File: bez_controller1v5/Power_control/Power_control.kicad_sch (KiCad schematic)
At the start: 7 parts, among them J1 Screw_Terminal_01x02, J2 Screw_Terminal_01x02, J3 Screw_Terminal_01x02, Q2 IRF4905STRLPBF

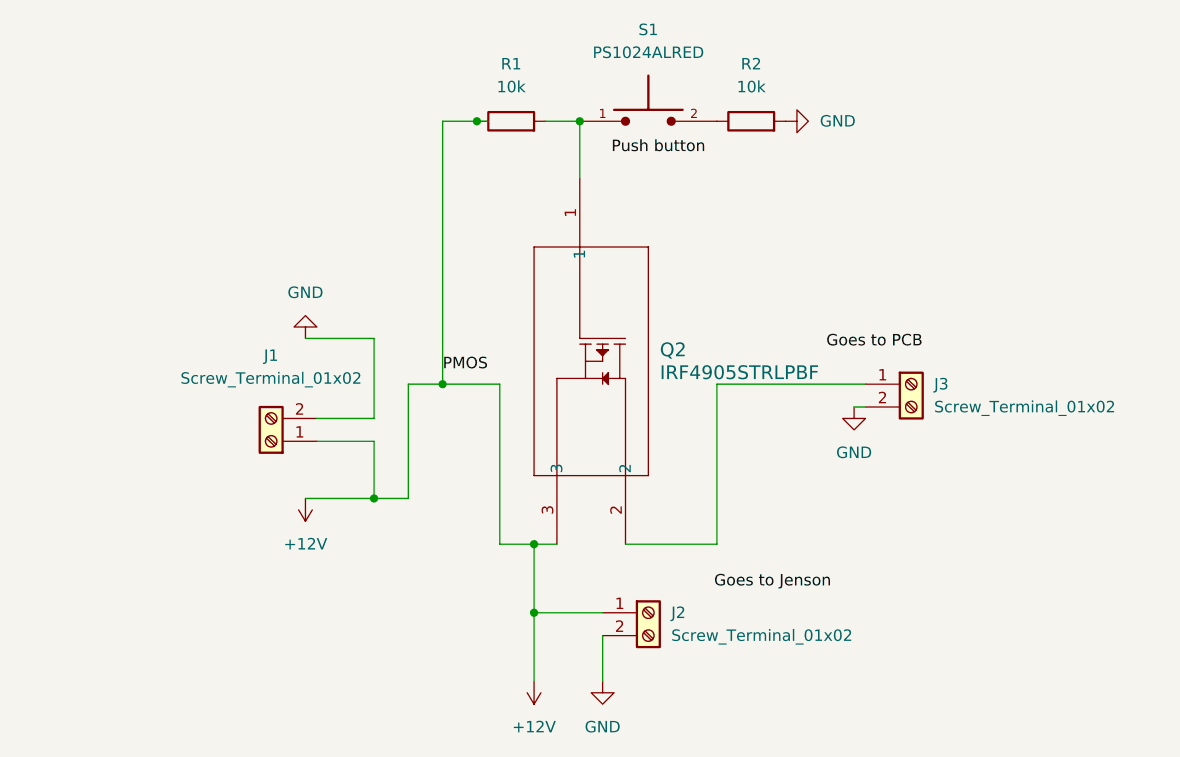
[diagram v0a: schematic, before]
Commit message: Cleaned circuit up a little
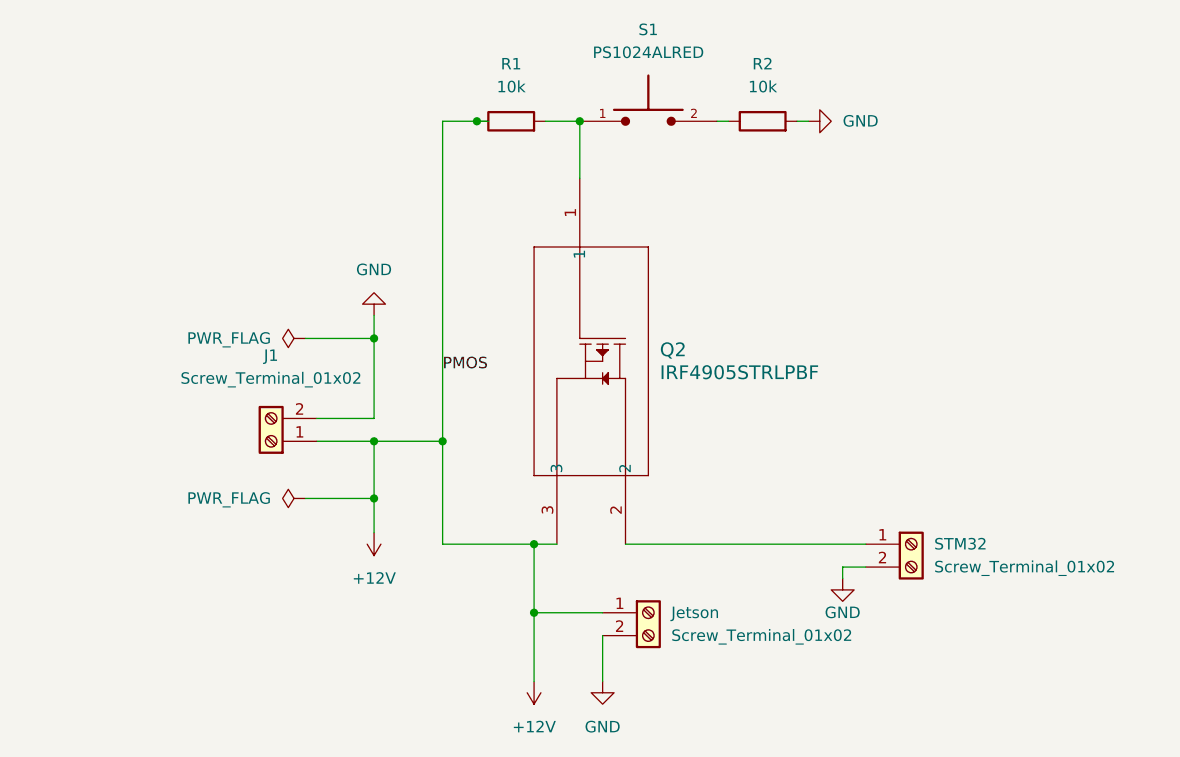
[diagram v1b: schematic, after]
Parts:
- renumbered J2 to Jetson, J3 to STM32
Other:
- moved on the sheet: R2, STM32

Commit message: Made foorprints and PCB for button
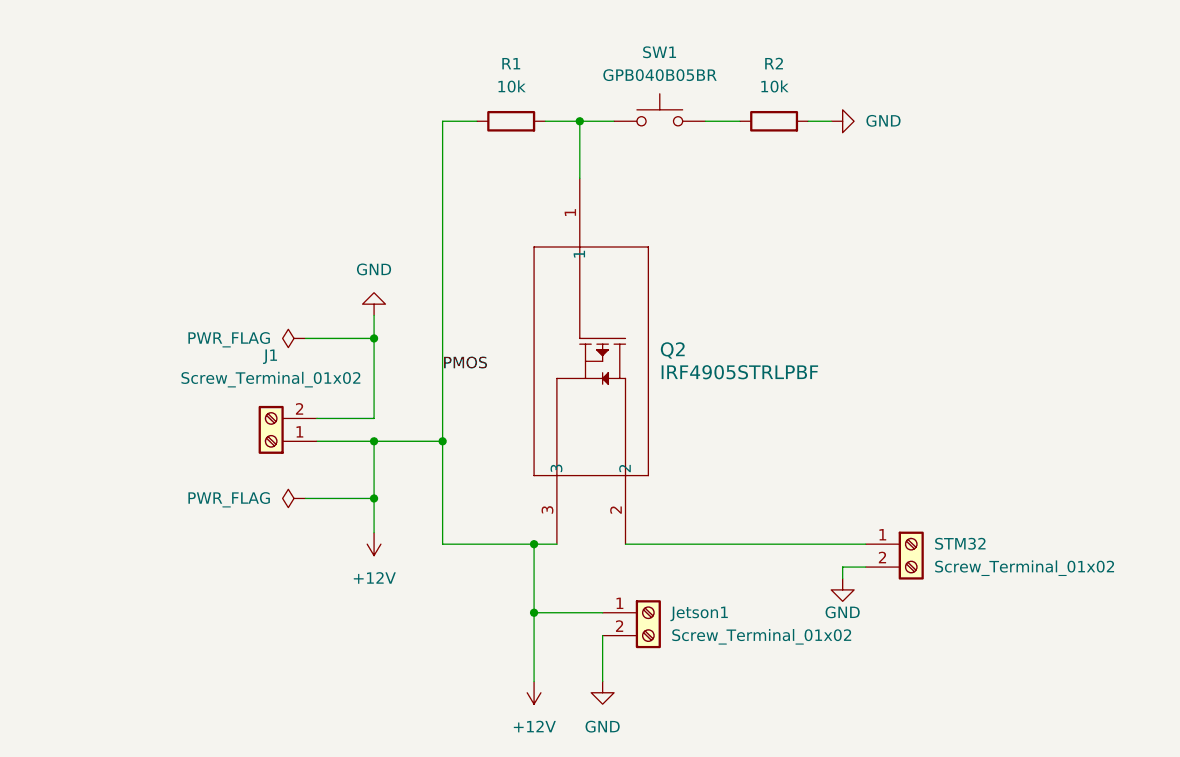
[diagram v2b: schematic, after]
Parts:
- removed S1: PS1024ALRED, PS1024ALRED:SW_PS1024ALRED, symbol PS1024ALRED:PS1024ALRED
- added SW1: GPB040B05BR, Library:GPB040B05BR, symbol Switch:SW_Push
- Q2: footprint TRAN_IRF4905STRLPBF_INF -> Library:IRF4905
- R1, R2: footprint (none) -> Resistor_SMD:R_0603_1608Metric
- renumbered Jetson to Jetson1
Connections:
- net at Q2.1, R1.2: now also SW1.1
- net at R2.1: now also SW1.2
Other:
- moved on the sheet: R2
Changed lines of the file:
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@@
 		(color 0 0 0 0)
 	)
-	(junction
-		(at 81.28 52.07)
-		(diameter 0)
-		(color 0 0 0 0)
-	)
 	(wire
 		(pts
@@
 	(wire
 		(pts
-			(xy 82.55 52.07) (xy 81.28 52.07)
-		)
-		(stroke
-			(width 0)
-			(type default)
-		)
-	)
-	(wire
-		(pts
 			(xy 87.63 106.68) (xy 87.63 99.06)
 		)
@@
 	(wire
 		(pts
+			(xy 120.65 52.07) (xy 118.11 52.07)
+		)
+		(stroke
+			(width 0)
+			(type default)
+		)
+	)
+	(wire
+		(pts
 			(xy 69.85 87.63) (xy 63.5 87.63)
 		)
@@
 	(wire
 		(pts
-			(xy 109.22 52.07) (xy 107.95 52.07)
-		)
-		(stroke
-			(width 0)
-			(type default)
-		)
-	)
-	(wire
-		(pts
 			(xy 69.85 93.98) (xy 69.85 97.79)
 		)
@@
 	(wire
 		(pts
-			(xy 116.84 52.07) (xy 118.11 52.07)
+			(xy 92.71 52.07) (xy 92.71 58.42)
 		)
 		(stroke
@@
 	(wire
 		(pts
+			(xy 106.68 52.07) (xy 110.49 52.07)
+		)
+		(stroke
+			(width 0)
+			(type default)
+		)
+	)
+	(wire
+		(pts
 			(xy 69.85 87.63) (xy 77.47 87.63)
 		)
@@
 	(wire
 		(pts
+			(xy 92.71 52.07) (xy 96.52 52.07)
+		)
+		(stroke
+			(width 0)
+			(type default)
+		)
+	)
+	(wire
+		(pts
 			(xy 81.28 52.07) (xy 77.47 52.07)
 		)
@@
 		(pts
 			(xy 62.23 76.2) (xy 69.85 76.2)
-		)
-		(stroke
-			(width 0)
-			(type default)
-		)
-	)
-	(wire
-		(pts
-			(xy 92.71 58.42) (xy 92.71 52.07)
 		)
 		(stroke
@@
 	)
 	(symbol
-		(lib_id "PS1024ALRED:PS1024ALRED")
-		(at 100.33 52.07 0)
-		(unit 1)
-		(exclude_from_sim no)
-		(in_bom yes)
-		(on_board yes)
-		(dnp no)
-		(fields_autoplaced yes)
-		(property "Reference" "S1"
-			(at 100.33 41.91 0)
-			(effects
-				(font
-					(size 1.27 1.27)
-				)
-			)
-		)
-		(property "Value" "PS1024ALRED"
-			(at 100.33 44.45 0)
-			(effects
-				(font
-					(size 1.27 1.27)
-				)
-			)
-		)
-		(property "Footprint" "PS1024ALRED:SW_PS1024ALRED"
-			(at 100.33 52.07 0)
-			(effects
-				(font
-					(size 1.27 1.27)
-				)
-				(justify bottom)
-				(hide yes)
-			)
-		)
-		(property "Datasheet" ""
-			(at 100.33 52.07 0)
-			(effects
-				(font
-					(size 1.27 1.27)
-				)
-				(hide yes)
-			)
-		)
-		(property "Description" ""
-			(at 100.33 52.07 0)
-			(effects
-				(font
-					(size 1.27 1.27)
-				)
-				(hide yes)
-			)
-		)
-		(property "PARTREV" "C"
-			(at 100.33 52.07 0)
-			(effects
-				(font
-					(size 1.27 1.27)
-				)
-				(justify bottom)
-				(hide yes)
-			)
-		)
-		(property "STANDARD" "IPC-7351B"
-			(at 100.33 52.07 0)
-			(effects
-				(font
-					(size 1.27 1.27)
-				)
-				(justify bottom)
-				(hide yes)
-			)
-		)
-		(property "MAXIMUM_PACKAGE_HEIGHT" "26.6 mm"
-			(at 100.33 52.07 0)
-			(effects
-				(font
-					(size 1.27 1.27)
-				)
-				(justify bottom)
-				(hide yes)
-			)
-		)
-		(property "MANUFACTURER" "E-Switch"
-			(at 100.33 52.07 0)
-			(effects
-				(font
-					(size 1.27 1.27)
-				)
-				(justify bottom)
-				(hide yes)
-			)
-		)
-		(pin "1"
-		)
-		(pin "2"
-		)
-		(instances
-			(project "Power_control"
-				(path "/56259e4c-5c8f-4073-95b8-1c3757b66f06"
-					(reference "S1")
-					(unit 1)
-				)
-			)
-		)
-	)
-	(symbol
 		(lib_id "Connector:Screw_Terminal_01x02")
 		(at 58.42 87.63 180)
@@
 			)
 		)
-		(property "Footprint" ""
+		(property "Footprint" "Resistor_SMD:R_0603_1608Metric"
 			(at 85.09 53.848 90)
 			(effects
@@
 	(symbol
 		(lib_id "power:GND")
-		(at 118.11 52.07 90)
+		(at 120.65 52.07 90)
 		(unit 1)
 		(exclude_from_sim no)
@@
 		(fields_autoplaced yes)
 		(property "Reference" "#PWR04"
-			(at 124.46 52.07 0)
+			(at 127 52.07 0)
 			(effects
 				(font
@@
 		)
 		(property "Value" "GND"
-			(at 121.92 52.0699 90)
+			(at 124.46 52.0699 90)
 			(effects
 				(font
@@
 		)
 		(property "Footprint" ""
-			(at 118.11 52.07 0)
+			(at 120.65 52.07 0)
 			(effects
 				(font
@@
 		)
 		(property "Datasheet" ""
-			(at 118.11 52.07 0)
+			(at 120.65 52.07 0)
 			(effects
 				(font
@@
 		)
 		(property "Description" "Power symbol creates a global label with name \"GND\" , ground"
-			(at 118.11 52.07 0)
+			(at 120.65 52.07 0)
 			(effects
 				(font
@@
 				(path "/56259e4c-5c8f-4073-95b8-1c3757b66f06"
 					(reference "#PWR04")
+					(unit 1)
+				)
+			)
+		)
+	)
+	(symbol
+		(lib_id "Switch:SW_Push")
+		(at 101.6 52.07 0)
+		(unit 1)
+		(exclude_from_sim no)
+		(in_bom yes)
+		(on_board yes)
+		(dnp no)
+		(fields_autoplaced yes)
+		(property "Reference" "SW1"
+			(at 101.6 44.45 0)
+			(effects
+				(font
+					(size 1.27 1.27)
+				)
+			)
+		)
+		(property "Value" "GPB040B05BR"
+			(at 101.6 46.99 0)
+			(effects
+				(font
+					(size 1.27 1.27)
+				)
+			)
+		)
+		(property "Footprint" "Library:GPB040B05BR"
+			(at 101.6 46.99 0)
+			(effects
+				(font
+					(size 1.27 1.27)
+				)
+				(hide yes)
+			)
+		)
+		(property "Datasheet" "~"
+			(at 101.6 46.99 0)
+			(effects
+				(font
+					(size 1.27 1.27)
+				)
+				(hide yes)
+			)
+		)
+		(property "Description" "Push button switch, generic, two pins"
+			(at 101.6 52.07 0)
+			(effects
+				(font
+					(size 1.27 1.27)
+				)
+				(hide yes)
+			)
+		)
+		(pin "1"
+		)
+		(pin "2"
+		)
+		(instances
+			(project ""
+				(path "/56259e4c-5c8f-4073-95b8-1c3757b66f06"
+					(reference "SW1")
 					(unit 1)
 				)
@@
 		(dnp no)
 		(fields_autoplaced yes)
-		(property "Reference" "Jetson"
+		(property "Reference" "Jetson1"
 			(at 102.87 106.6799 0)
 			(effects
@@
 			(project "Power_control"
 				(path "/56259e4c-5c8f-4073-95b8-1c3757b66f06"
-					(reference "Jetson")
+					(reference "Jetson1")
 					(unit 1)
 				)
@@
 	(symbol
 		(lib_id "Device:R")
-		(at 113.03 52.07 90)
+		(at 114.3 52.07 90)
 		(unit 1)
 		(exclude_from_sim no)
@@
 		(fields_autoplaced yes)
 		(property "Reference" "R2"
-			(at 113.03 45.72 90)
+			(at 114.3 45.72 90)
 			(effects
 				(font
@@
 		)
 		(property "Value" "10k"
-			(at 113.03 48.26 90)
-			(effects
-				(font
-					(size 1.27 1.27)
-				)
-			)
-		)
-		(property "Footprint" ""
-			(at 113.03 53.848 90)
+			(at 114.3 48.26 90)
+			(effects
+				(font
+					(size 1.27 1.27)
+				)
+			)
+		)
+		(property "Footprint" "Resistor_SMD:R_0603_1608Metric"
+			(at 114.3 53.848 90)
 			(effects
 				(font
@@
 		)
 		(property "Datasheet" "~"
-			(at 113.03 52.07 0)
+			(at 114.3 52.07 0)
 			(effects
 				(font
@@
 		)
 		(property "Description" "Resistor"
-			(at 113.03 52.07 0)
+			(at 114.3 52.07 0)
 			(effects
 				(font
@@
 			)
 		)
-		(property "Footprint" "TRAN_IRF4905STRLPBF_INF"
+		(property "Footprint" "Library:IRF4905"
 			(at 95.25 58.42 0)
 			(effects

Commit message: Fixed XT60 polarity
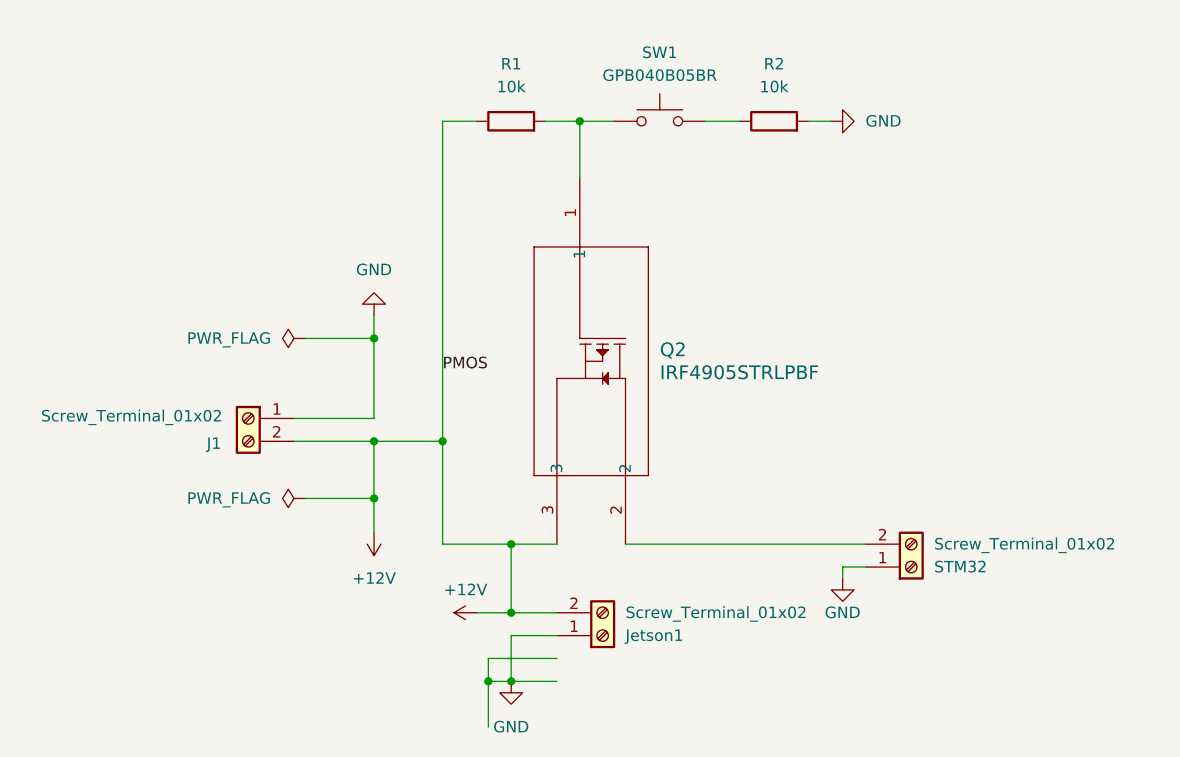
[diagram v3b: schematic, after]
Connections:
- net +12V: now also J1.2 (Pin_2), Jetson1.2 (Pin_2); no longer J1.1 (Pin_1), Jetson1.1 (Pin_1)
- net GND: now also J1.1 (Pin_1), Jetson1.1 (Pin_1), STM32.1 (Pin_1); no longer J1.2 (Pin_2), Jetson1.2 (Pin_2), STM32.2 (Pin_2)
- net at Q2.2: now also STM32.2 (Pin_2); no longer STM32.1 (Pin_1)
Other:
- moved on the sheet: J1, Jetson1
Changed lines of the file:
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@@
 	(paper "A4")
+	(junction
+		(at 82.55 114.3)
+		(diameter 0)
+		(color 0 0 0 0)
+	)
 	(junction
 		(at 77.47 87.63)
@@
 	)
 	(junction
-		(at 87.63 106.68)
+		(at 69.85 87.63)
 		(diameter 0)
 		(color 0 0 0 0)
@@
 	)
 	(junction
-		(at 87.63 99.06)
+		(at 85.09 114.3)
 		(diameter 0)
 		(color 0 0 0 0)
 	)
 	(junction
-		(at 69.85 87.63)
+		(at 85.09 106.68)
+		(diameter 0)
+		(color 0 0 0 0)
+	)
+	(junction
+		(at 85.09 99.06)
 		(diameter 0)
 		(color 0 0 0 0)
@@
 	(wire
 		(pts
-			(xy 87.63 106.68) (xy 87.63 114.3)
-		)
-		(stroke
-			(width 0)
-			(type default)
-		)
-	)
-	(wire
-		(pts
-			(xy 87.63 106.68) (xy 87.63 99.06)
+			(xy 85.09 99.06) (xy 90.17 99.06)
+		)
+		(stroke
+			(width 0)
+			(type default)
+		)
+	)
+	(wire
+		(pts
+			(xy 85.09 99.06) (xy 85.09 106.68)
 		)
 		(stroke
@@
 	(wire
 		(pts
-			(xy 69.85 87.63) (xy 63.5 87.63)
+			(xy 82.55 111.76) (xy 82.55 114.3)
+		)
+		(stroke
+			(width 0)
+			(type default)
+		)
+	)
+	(wire
+		(pts
+			(xy 82.55 114.3) (xy 82.55 119.38)
+		)
+		(stroke
+			(width 0)
+			(type default)
+		)
+	)
+	(wire
+		(pts
+			(xy 97.79 99.06) (xy 124.46 99.06)
 		)
 		(stroke
@@
 	(wire
 		(pts
-			(xy 77.47 99.06) (xy 87.63 99.06)
-		)
-		(stroke
-			(width 0)
-			(type default)
-		)
-	)
-	(wire
-		(pts
-			(xy 97.79 99.06) (xy 124.46 99.06)
+			(xy 77.47 99.06) (xy 85.09 99.06)
 		)
 		(stroke
@@
 	(wire
 		(pts
+			(xy 60.96 85.09) (xy 69.85 85.09)
+		)
+		(stroke
+			(width 0)
+			(type default)
+		)
+	)
+	(wire
+		(pts
 			(xy 69.85 87.63) (xy 77.47 87.63)
 		)
@@
 	(wire
 		(pts
-			(xy 87.63 99.06) (xy 90.17 99.06)
+			(xy 121.92 101.6) (xy 124.46 101.6)
+		)
+		(stroke
+			(width 0)
+			(type default)
+		)
+	)
+	(wire
+		(pts
+			(xy 85.09 114.3) (xy 85.09 109.22)
 		)
 		(stroke
@@
 	(wire
 		(pts
+			(xy 82.55 114.3) (xy 85.09 114.3)
+		)
+		(stroke
+			(width 0)
+			(type default)
+		)
+	)
+	(wire
+		(pts
 			(xy 77.47 87.63) (xy 77.47 99.06)
 		)
@@
 	(wire
 		(pts
-			(xy 87.63 106.68) (xy 95.25 106.68)
-		)
-		(stroke
-			(width 0)
-			(type default)
-		)
-	)
-	(wire
-		(pts
 			(xy 77.47 52.07) (xy 77.47 87.63)
 		)
@@
 	(wire
 		(pts
+			(xy 81.28 106.68) (xy 85.09 106.68)
+		)
+		(stroke
+			(width 0)
+			(type default)
+		)
+	)
+	(wire
+		(pts
 			(xy 81.28 52.07) (xy 77.47 52.07)
 		)
@@
 	(wire
 		(pts
+			(xy 85.09 114.3) (xy 90.17 114.3)
+		)
+		(stroke
+			(width 0)
+			(type default)
+		)
+	)
+	(wire
+		(pts
 			(xy 69.85 76.2) (xy 69.85 85.09)
 		)
@@
 	(wire
 		(pts
-			(xy 95.25 109.22) (xy 95.25 114.3)
+			(xy 85.09 109.22) (xy 90.17 109.22)
 		)
 		(stroke
@@
 	(wire
 		(pts
-			(xy 69.85 85.09) (xy 63.5 85.09)
-		)
-		(stroke
-			(width 0)
-			(type default)
-		)
-	)
-	(wire
-		(pts
-			(xy 121.92 101.6) (xy 124.46 101.6)
+			(xy 60.96 87.63) (xy 69.85 87.63)
 		)
 		(stroke
@@
 		(pts
 			(xy 62.23 76.2) (xy 69.85 76.2)
+		)
+		(stroke
+			(width 0)
+			(type default)
+		)
+	)
+	(wire
+		(pts
+			(xy 85.09 106.68) (xy 90.17 106.68)
+		)
+		(stroke
+			(width 0)
+			(type default)
+		)
+	)
+	(wire
+		(pts
+			(xy 82.55 111.76) (xy 90.17 111.76)
 		)
 		(stroke
@@
 	(symbol
 		(lib_id "Connector:Screw_Terminal_01x02")
-		(at 58.42 87.63 180)
-		(unit 1)
-		(exclude_from_sim no)
-		(in_bom yes)
-		(on_board yes)
-		(dnp no)
-		(fields_autoplaced yes)
+		(at 55.88 85.09 0)
+		(mirror y)
+		(unit 1)
+		(exclude_from_sim no)
+		(in_bom yes)
+		(on_board yes)
+		(dnp no)
 		(property "Reference" "J1"
-			(at 58.42 78.105 0)
+			(at 52.07 87.884 0)
 			(effects
 				(font
@@
 		)
 		(property "Value" "Screw_Terminal_01x02"
-			(at 58.42 80.645 0)
+			(at 42.926 84.836 0)
 			(effects
 				(font
@@
 		)
 		(property "Footprint" "Connector_AMASS:AMASS_XT60PW-F_1x02_P7.20mm_Horizontal"
-			(at 58.42 87.63 0)
+			(at 55.88 85.09 0)
 			(effects
 				(font
@@
 		)
 		(property "Datasheet" "~"
-			(at 58.42 87.63 0)
+			(at 55.88 85.09 0)
 			(effects
 				(font
@@
 		)
 		(property "Description" ""
-			(at 58.42 87.63 0)
+			(at 55.88 85.09 0)
 			(effects
 				(font
@@
 	(symbol
 		(lib_id "power:GND")
-		(at 95.25 114.3 0)
+		(at 85.09 114.3 0)
 		(unit 1)
 		(exclude_from_sim no)
@@
 		(fields_autoplaced yes)
 		(property "Reference" "#PWR05"
-			(at 95.25 120.65 0)
+			(at 85.09 120.65 0)
 			(effects
 				(font
@@
 		)
 		(property "Value" "GND"
-			(at 95.25 119.38 0)
+			(at 85.09 119.38 0)
 			(effects
 				(font
@@
 		)
 		(property "Footprint" ""
-			(at 95.25 114.3 0)
+			(at 85.09 114.3 0)
 			(effects
 				(font
@@
 		)
 		(property "Datasheet" ""
-			(at 95.25 114.3 0)
+			(at 85.09 114.3 0)
 			(effects
 				(font
@@
 		)
 		(property "Description" "Power symbol creates a global label with name \"GND\" , ground"
-			(at 95.25 114.3 0)
+			(at 85.09 114.3 0)
 			(effects
 				(font
@@
 	(symbol
 		(lib_id "Connector:Screw_Terminal_01x02")
-		(at 100.33 106.68 0)
-		(unit 1)
-		(exclude_from_sim no)
-		(in_bom yes)
-		(on_board yes)
-		(dnp no)
-		(fields_autoplaced yes)
+		(at 95.25 109.22 0)
+		(mirror x)
+		(unit 1)
+		(exclude_from_sim no)
+		(in_bom yes)
+		(on_board yes)
+		(dnp no)
 		(property "Reference" "Jetson1"
-			(at 102.87 106.6799 0)
+			(at 97.79 109.2201 0)
 			(effects
 				(font
@@
 		)
 		(property "Value" "Screw_Terminal_01x02"
-			(at 102.87 109.2199 0)
+			(at 97.79 106.6801 0)
 			(effects
 				(font
@@
 		)
 		(property "Footprint" "Connector_AMASS:AMASS_XT60PW-F_1x02_P7.20mm_Horizontal"
-			(at 100.33 106.68 0)
+			(at 95.25 109.22 0)
 			(effects
 				(font
@@
 		)
 		(property "Datasheet" "~"
-			(at 100.33 106.68 0)
+			(at 95.25 109.22 0)
 			(effects
 				(font
@@
 		)
 		(property "Description" ""
-			(at 100.33 106.68 0)
+			(at 95.25 109.22 0)
 			(effects
 				(font
@@
 	(symbol
 		(lib_id "Connector:Screw_Terminal_01x02")
-		(at 129.54 99.06 0)
-		(unit 1)
-		(exclude_from_sim no)
-		(in_bom yes)
-		(on_board yes)
-		(dnp no)
-		(fields_autoplaced yes)
+		(at 129.54 101.6 0)
+		(mirror x)
+		(unit 1)
+		(exclude_from_sim no)
+		(in_bom yes)
+		(on_board yes)
+		(dnp no)
 		(property "Reference" "STM32"
-			(at 132.08 99.0599 0)
+			(at 132.08 101.6001 0)
 			(effects
 				(font
@@
 		)
 		(property "Value" "Screw_Terminal_01x02"
-			(at 132.08 101.5999 0)
+			(at 132.08 99.0601 0)
 			(effects
 				(font
@@
 		)
 		(property "Footprint" "Connector_AMASS:AMASS_XT60PW-F_1x02_P7.20mm_Horizontal"
-			(at 129.54 99.06 0)
+			(at 129.54 101.6 0)
 			(effects
 				(font
@@
 		)
 		(property "Datasheet" "~"
-			(at 129.54 99.06 0)
+			(at 129.54 101.6 0)
 			(effects
 				(font
@@
 		)
 		(property "Description" ""
-			(at 129.54 99.06 0)
+			(at 129.54 101.6 0)
 			(effects
 				(font
@@
 	(symbol
 		(lib_id "power:+12V")
-		(at 87.63 114.3 180)
+		(at 81.28 106.68 90)
 		(unit 1)
 		(exclude_from_sim no)
@@
 		(fields_autoplaced yes)
 		(property "Reference" "#PWR03"
-			(at 87.63 110.49 0)
+			(at 85.09 106.68 0)
 			(effects
 				(font
@@
 		)
 		(property "Value" "+12V"
-			(at 87.63 119.38 0)
+			(at 80.01 104.14 90)
 			(effects
 				(font
@@
 		)
 		(property "Footprint" ""
-			(at 87.63 114.3 0)
+			(at 81.28 106.68 0)
 			(effects
 				(font
@@
 		)
 		(property "Datasheet" ""
-			(at 87.63 114.3 0)
+			(at 81.28 106.68 0)
 			(effects
 				(font
@@
 		)
 		(property "Description" "Power symbol creates a global label with name \"+12V\""
-			(at 87.63 114.3 0)
-			(effects
-				(font
+			(at 81.28 106.68 0)
+			(effects
+				(font
